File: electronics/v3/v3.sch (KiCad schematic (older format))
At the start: 43 parts, among them IC101 ArduinoProMini, J104 Conn_02x02_Odd_Even, J106 Conn_01x03_Female, Q101 PN2222A, Q102 PN2222A, U101 L7805

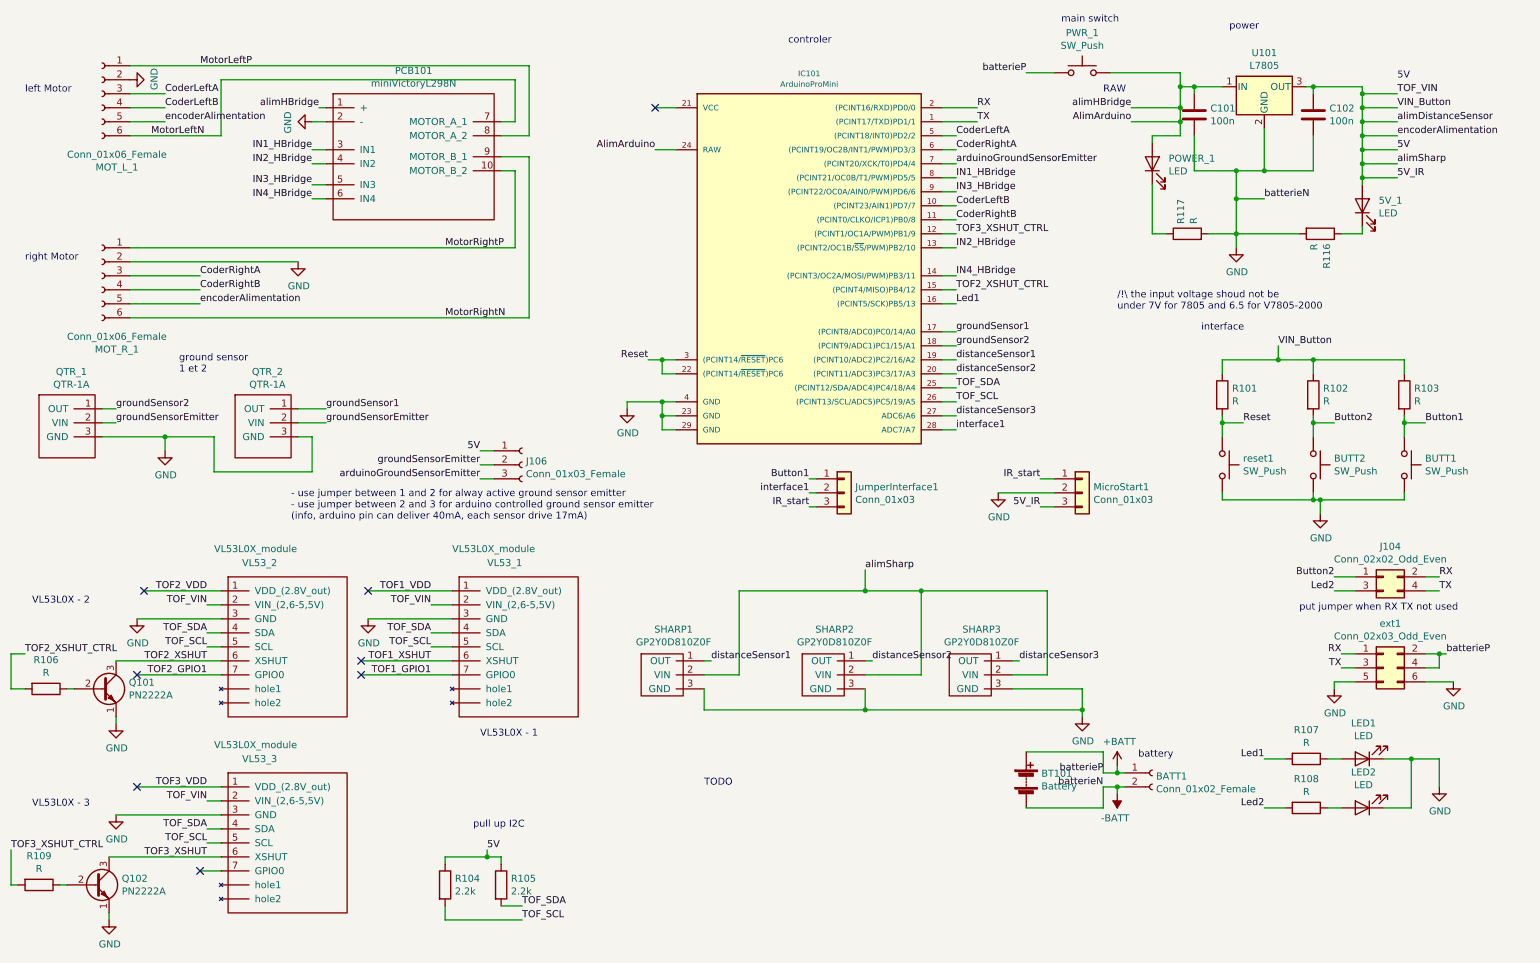
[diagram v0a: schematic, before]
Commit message: add mechanical part, first test not working, need to be redisign
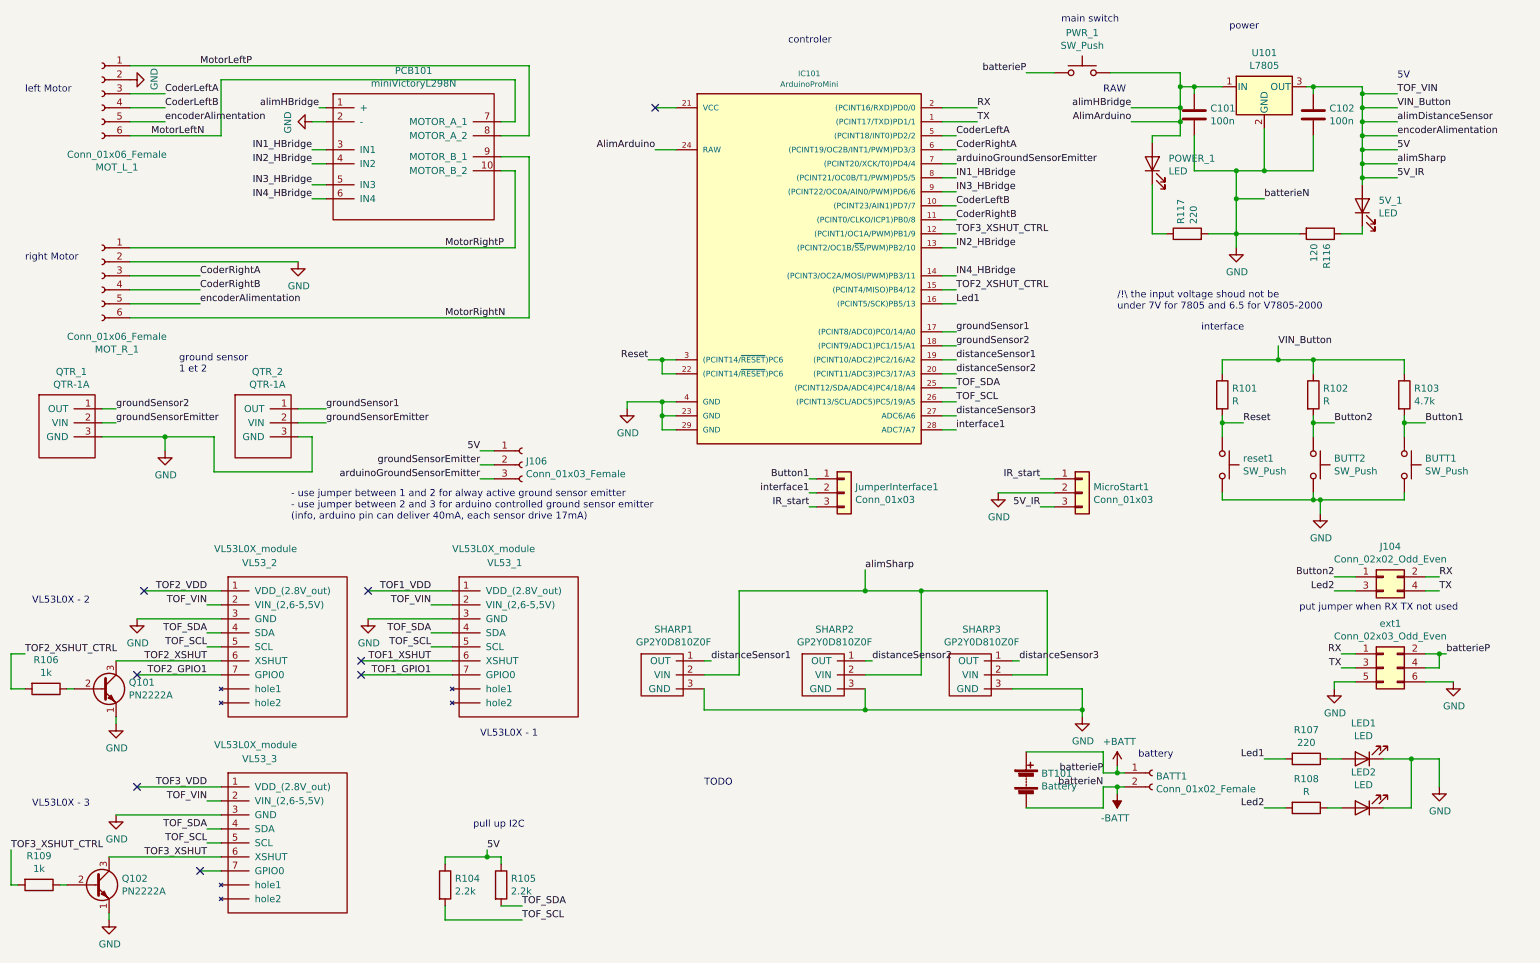
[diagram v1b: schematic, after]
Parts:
- R103: value R -> 4.7k
- R106, R109: value R -> 1k
- R107, R117: value R -> 220
- R116: value R -> 120
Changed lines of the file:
@@
 P 10550 3350
 F 0 "R103" H 10620 3396 50  0000 L CNN
-F 1 "R" H 10620 3305 50  0000 L CNN
+F 1 "4.7k" H 10620 3305 50  0000 L CNN
 F 2 "Resistors_THT:R_Axial_DIN0207_L6.3mm_D2.5mm_P10.16mm_Horizontal" V 10480 3350 50  0001 C CNN
 F 3 "~" H 10550 3350 50  0001 C CNN
@@
 P 9850 5950
 F 0 "R107" V 9643 5950 50  0000 C CNN
-F 1 "R" V 9734 5950 50  0000 C CNN
+F 1 "220" V 9734 5950 50  0000 C CNN
 F 2 "Resistors_THT:R_Axial_DIN0207_L6.3mm_D2.5mm_P10.16mm_Horizontal" V 9780 5950 50  0001 C CNN
 F 3 "~" H 9850 5950 50  0001 C CNN
@@
 P 9950 2200
 F 0 "R116" H 10020 2246 50  0000 L CNN
-F 1 "R" H 10020 2155 50  0000 L CNN
+F 1 "120" H 10020 2155 50  0000 L CNN
 F 2 "Resistors_THT:R_Axial_DIN0207_L6.3mm_D2.5mm_P10.16mm_Horizontal" V 9880 2200 50  0001 C CNN
 F 3 "~" H 9950 2200 50  0001 C CNN
@@
 P 9000 2200
 F 0 "R117" H 9070 2246 50  0000 L CNN
-F 1 "R" H 9070 2155 50  0000 L CNN
+F 1 "220" H 9070 2155 50  0000 L CNN
 F 2 "Resistors_THT:R_Axial_DIN0207_L6.3mm_D2.5mm_P10.16mm_Horizontal" V 8930 2200 50  0001 C CNN
 F 3 "~" H 9000 2200 50  0001 C CNN
@@
 P 800 6850
 F 0 "R109" V 593 6850 50  0000 C CNN
-F 1 "R" V 684 6850 50  0000 C CNN
+F 1 "1k" V 684 6850 50  0000 C CNN
 F 2 "Resistors_THT:R_Axial_DIN0207_L6.3mm_D2.5mm_P10.16mm_Horizontal" V 730 6850 50  0001 C CNN
 F 3 "~" H 800 6850 50  0001 C CNN
@@
 P 850 5450
 F 0 "R106" V 643 5450 50  0000 C CNN
-F 1 "R" V 734 5450 50  0000 C CNN
+F 1 "1k" V 734 5450 50  0000 C CNN
 F 2 "Resistors_THT:R_Axial_DIN0207_L6.3mm_D2.5mm_P10.16mm_Horizontal" V 780 5450 50  0001 C CNN
 F 3 "~" H 850 5450 50  0001 C CNN
